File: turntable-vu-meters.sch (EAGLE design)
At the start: 26 parts, among them IC1 LM3914N, IC2 LM3914N, IC3 7805TV

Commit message: Finish up schematic, add values for components
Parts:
- removed R10, R9: (no value), rcl:R-EU_0204/7
- C5, C7: value (none) -> 470µF
- C6, C8: value (none) -> 220µF; device rcl:CPOL-EUE3.5-8 -> rcl:CPOL-EUE2.5-7
- R1, R2: value (none) -> 820Ω
- R3, R4: value (none) -> 10kΩ
- R5: value 10k -> 220Ω
- R6: value 10k -> 1kΩ
- R7: value (none) -> 220Ω
- R8: value (none) -> 1kΩ
- T1, T2: value (none) -> A852 8XA
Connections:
- net +12V renamed N$27
- removed net GND: C1.-, C2.-, IC1.RLO, IC1.V-, IC2.RLO, IC2.V-, IC3.GND, R2.1, R4.1, R5.2, R6.1, SV1.4, T1.C, T2.C
- removed net N$27 (its old number): IC2.REFADJ, R3.1, R4.2
- net N$16: now also R7.2; no longer R9.2
- net N$21: now also R6.2; no longer R8.2
- net N$22: now also R3.1; no longer R5.1
- net N$23: now also R4.2; no longer R6.2
- net N$25: now also R2.2; no longer R3.2
- net N$26: now also C1.-, C2.-, IC1.RLO, IC1.V-, IC2.REFADJ, IC2.RLO, IC2.V-, IC3.GND, R2.1, R3.2, R4.1, SV1.4, T1.C, T2.C; no longer R2.2
- net N$30: now also R6.1; no longer R8.1
- net N$32: now also R5.1; no longer R7.1
- net N$33: now also R8.2; no longer R10.2
- net N$34: now also R8.1; no longer R10.1
- net N$35: now also R7.1; no longer R9.1
- net N$6: now also R5.2; no longer R7.2
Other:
- moved on the sheet: R2, R3, R4, R5, R6, R7, R8

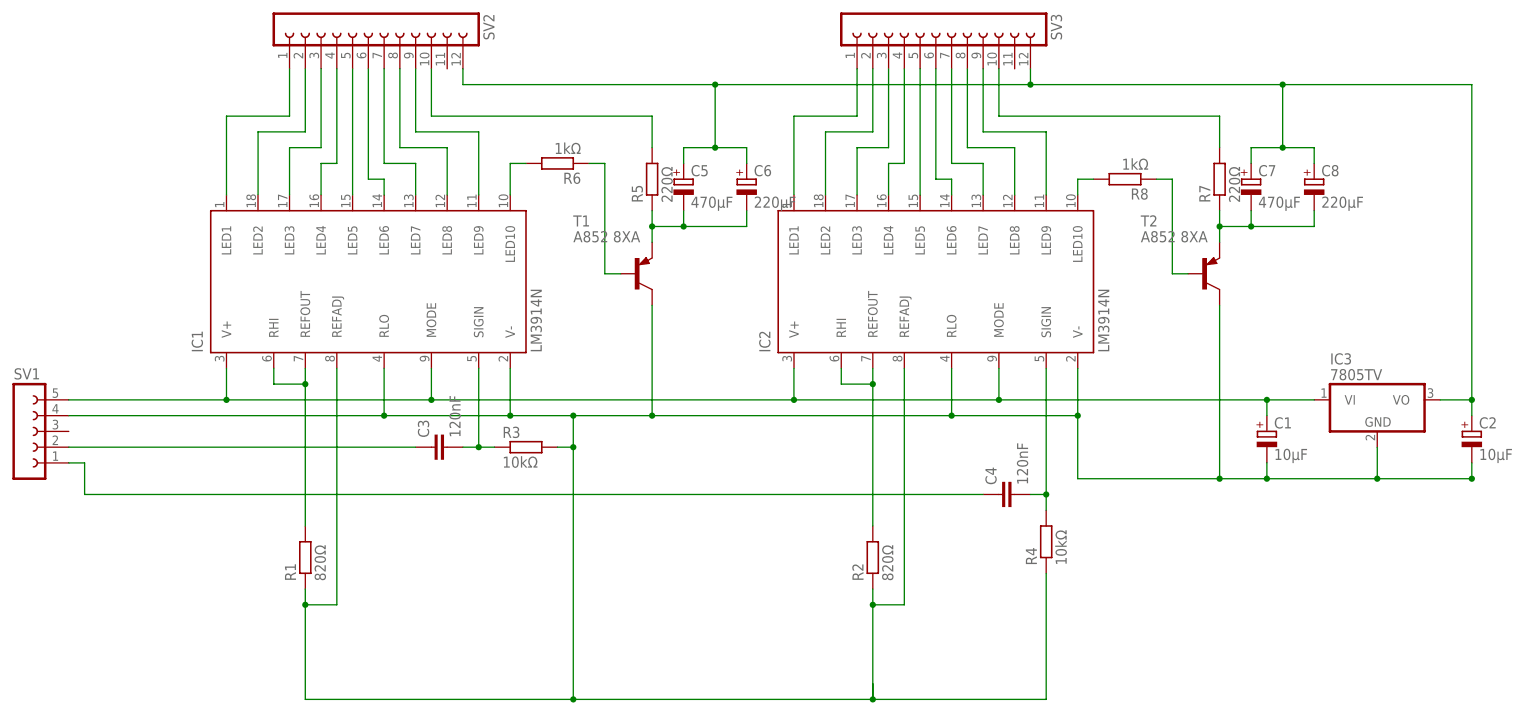
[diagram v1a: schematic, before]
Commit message: Swap connectors
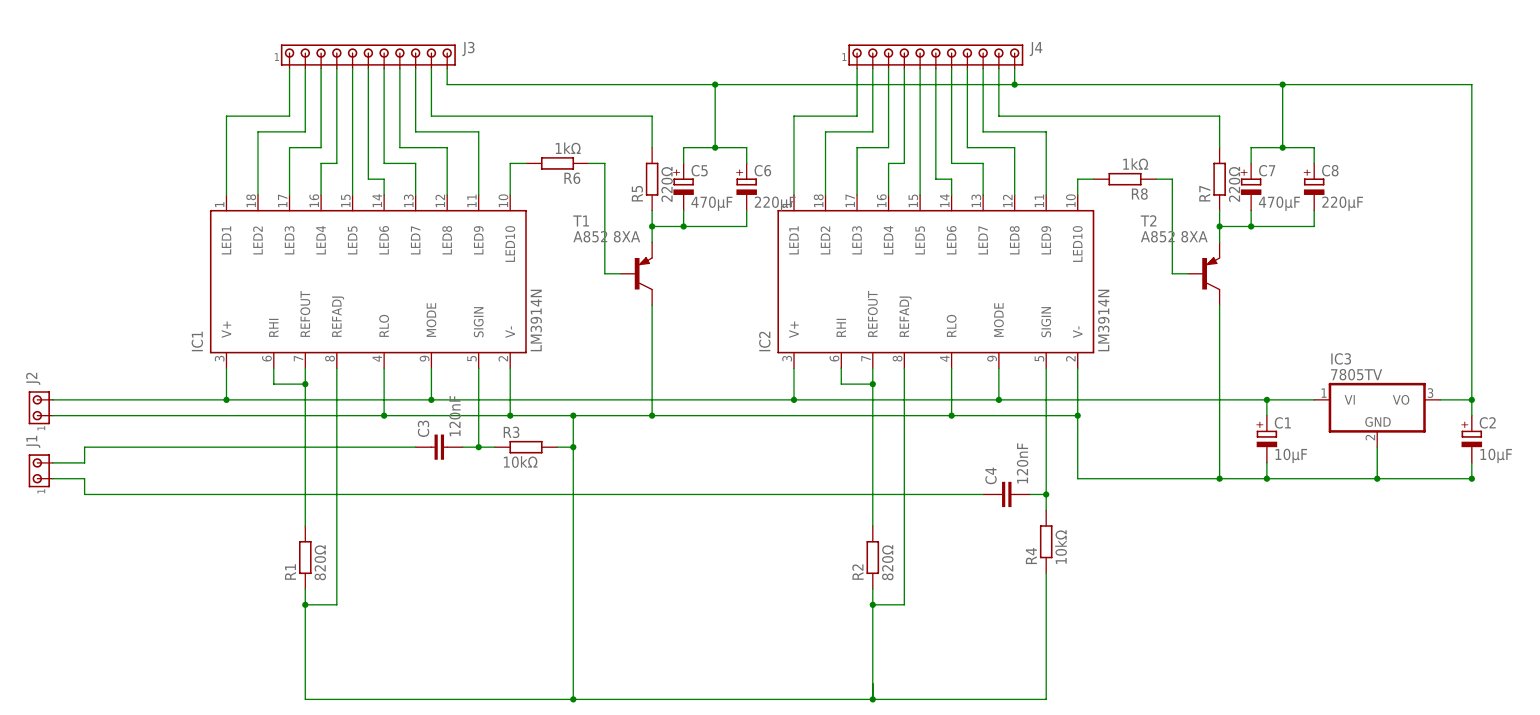
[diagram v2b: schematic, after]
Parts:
- removed SV1: (no value), con-lsta:FE05W
- removed SV2, SV3: (no value), con-lsta:FE12-1
- added J1, J2: (no value), con-amp:MTA02-156
- added J3, J4: (no value), con-amp:MTA11-156
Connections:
- net N$1: now also J3.1; no longer SV2.1
- net N$10: now also J3.6; no longer SV2.6
- net N$11: now also J4.1; no longer SV3.1
- net N$12: now also J4.2; no longer SV3.2
- net N$13: now also J4.3; no longer SV3.3
- net N$14: now also J4.4; no longer SV3.4
- net N$15: now also J4.5; no longer SV3.5
- net N$16: now also J4.10; no longer SV3.10
- net N$17: now also J4.9; no longer SV3.9
- net N$18: now also J4.8; no longer SV3.8
- net N$19: now also J4.7; no longer SV3.7
- net N$2: now also J3.2; no longer SV2.2
- net N$20: now also J4.6; no longer SV3.6
- net N$26: now also J2.1; no longer SV1.4
- net N$27: now also J2.2; no longer SV1.5
- net N$28: now also J1.1; no longer SV1.1
- net N$29: now also J1.2; no longer SV1.2
- net N$3: now also J3.3; no longer SV2.3
- net N$31: now also J3.11, J4.11; no longer SV2.12, SV3.12
- net N$4: now also J3.4; no longer SV2.4
- net N$5: now also J3.5; no longer SV2.5
- net N$6: now also J3.10; no longer SV2.10
- net N$7: now also J3.9; no longer SV2.9
- net N$8: now also J3.8; no longer SV2.8
- net N$9: now also J3.7; no longer SV2.7
